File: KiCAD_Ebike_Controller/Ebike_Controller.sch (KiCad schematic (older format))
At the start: 1 part

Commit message: close to being done, need to add current pull ups on i2c
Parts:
- removed J?: Conn_01x05_Male, symbol Connector:Conn_01x05_Male
- added J?: Conn_01x05_Male, symbol Connector:Conn_01x05_Male
- added J?: SWD Programming Pins, symbol Connector:Conn_01x05_Male
- added R?: 100k, symbol Device:R_Small
- added SW?: SW_Push, symbol Switch:SW_Push
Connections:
- net labels added: +48V, LSS
- wire segments 37 -> 65

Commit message: schem done
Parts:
- removed SW?: SW_Push, symbol Switch:SW_Push
- added C? (x2): 100n, symbol Device:C_Small
- added J?: Mode 2, symbol Connector:Conn_01x02_Female
- added J?: Mode 1, symbol Connector:Conn_01x02_Female
- added R?: 100k, symbol Device:R_Small
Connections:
- net labels added: BRAKE_SW_BP6, SWCLK, SWDIO, THROTTLE_PA2, nRST
- wire segments 65 -> 87
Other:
- moved on the sheet: R?

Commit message: adding footprints
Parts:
- removed J?: Conn_01x05_Male, symbol Connector:Conn_01x05_Male
- removed J?: SWD Programming Pins, symbol Connector:Conn_01x05_Male
- removed J?: Mode 2, symbol Connector:Conn_01x02_Female
- removed J?: Mode 1, symbol Connector:Conn_01x02_Female
- added C1: 100n, Capacitor_SMD:C_0805_2012Metric, symbol Device:C_Small
- added J1: IO, symbol Connector:Conn_01x06_Female
- added J2: Prog, symbol Connector:Conn_01x05_Female
- added J3: Hall Effect Sensors, symbol Connector:Screw_Terminal_01x05
- added J4: PHASE_A, symbol Connector:Screw_Terminal_01x01
- added J5: PHASE_B, symbol Connector:Screw_Terminal_01x01
- added J6: PHASE_C, symbol Connector:Screw_Terminal_01x01
- added R1: 100k, symbol Device:R_Small
- C2, C3: renamed from C?; footprint (none) -> Capacitor_SMD:C_0805_2012Metric_Pad1.15x1.40mm_HandSolder
- gave numbers to parts that had none: 2
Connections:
- net labels added: MODE1_SW_PB7, MODE2_SW_PA3
- wire segments 87 -> 88
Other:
- note added: "A"
- note added: "B"
- note added: "C"
- note added: "IO Pins"
- note added: "debounce filters"
- moved on the sheet: C2, C3, R2, R3

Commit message: 50% of the way through the layout
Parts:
- added C32: 50n, Capacitor_SMD:C_0805_2012Metric_Pad1.15x1.40mm_HandSolder, symbol Device:C_Small
- added J8: +48V, Power_Connector:180A_screw_terminal_7461383, symbol Connector:Screw_Terminal_01x01
- added J9: GND, Power_Connector:180A_screw_terminal_7461383, symbol Connector:Screw_Terminal_01x01
- added NT1: Net-Tie_3, NetTie:NetTie-3_THT_Pad1.0mm, symbol Device:Net-Tie_3
- added R45: 8.2k, Resistor_SMD:R_0805_2012Metric_Pad1.15x1.40mm_HandSolder, symbol Device:R_Small
- C1: footprint Capacitor_SMD:C_0805_2012Metric -> Capacitor_SMD:C_0805_2012Metric_Pad1.15x1.40mm_HandSolder
- J1: footprint (none) -> Connector_PinHeader_2.54mm:PinHeader_1x06_P2.54mm_Vertical
- J2: footprint (none) -> Connector_PinHeader_2.54mm:PinHeader_1x05_P2.54mm_Vertical
- J3: footprint (none) -> Connector_Phoenix_MC:PhoenixContact_MC_1,5_5-G-3.81_1x05_P3.81mm_Horizontal
- J4, J5, J6: footprint (none) -> Power_Connector:180A_screw_terminal_7461383
- R1, R2, R3: footprint (none) -> Resistor_SMD:R_0805_2012Metric_Pad1.15x1.40mm_HandSolder
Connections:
- net +48V: now also J8.1 (Pin_1)
- net GND: now also J9.1 (Pin_1), NT1.2; no longer C1.2, C2.2, C3.2, J1.6 (Pin_6), J2.5 (Pin_5), J3.5 (Pin_5)
- net MODE1_SW_PB7: now also J1.4 (Pin_4); no longer J1.5 (Pin_5)
- net MODE2_SW_PA3: now also J1.5 (Pin_5); no longer J1.4 (Pin_4)
- net THROTTLE_PA2: now also R45.1
- new net GNDA: C1.2, C2.2, C3.2, C32.2, NT1.1
- new net GNDD: J1.6 (Pin_6), J2.5 (Pin_5), J3.5 (Pin_5), NT1.3
- new net MCU/THROTTLE_PA2: C32.1, R45.2
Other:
- note added: "Battery\nInputs"
- note added: "Star ground connections"
- note added: "THROTTLE_PA2"
- note added: "low pass filter"
- moved on the sheet: C1, C2, C3, J1, R1, R2, R3

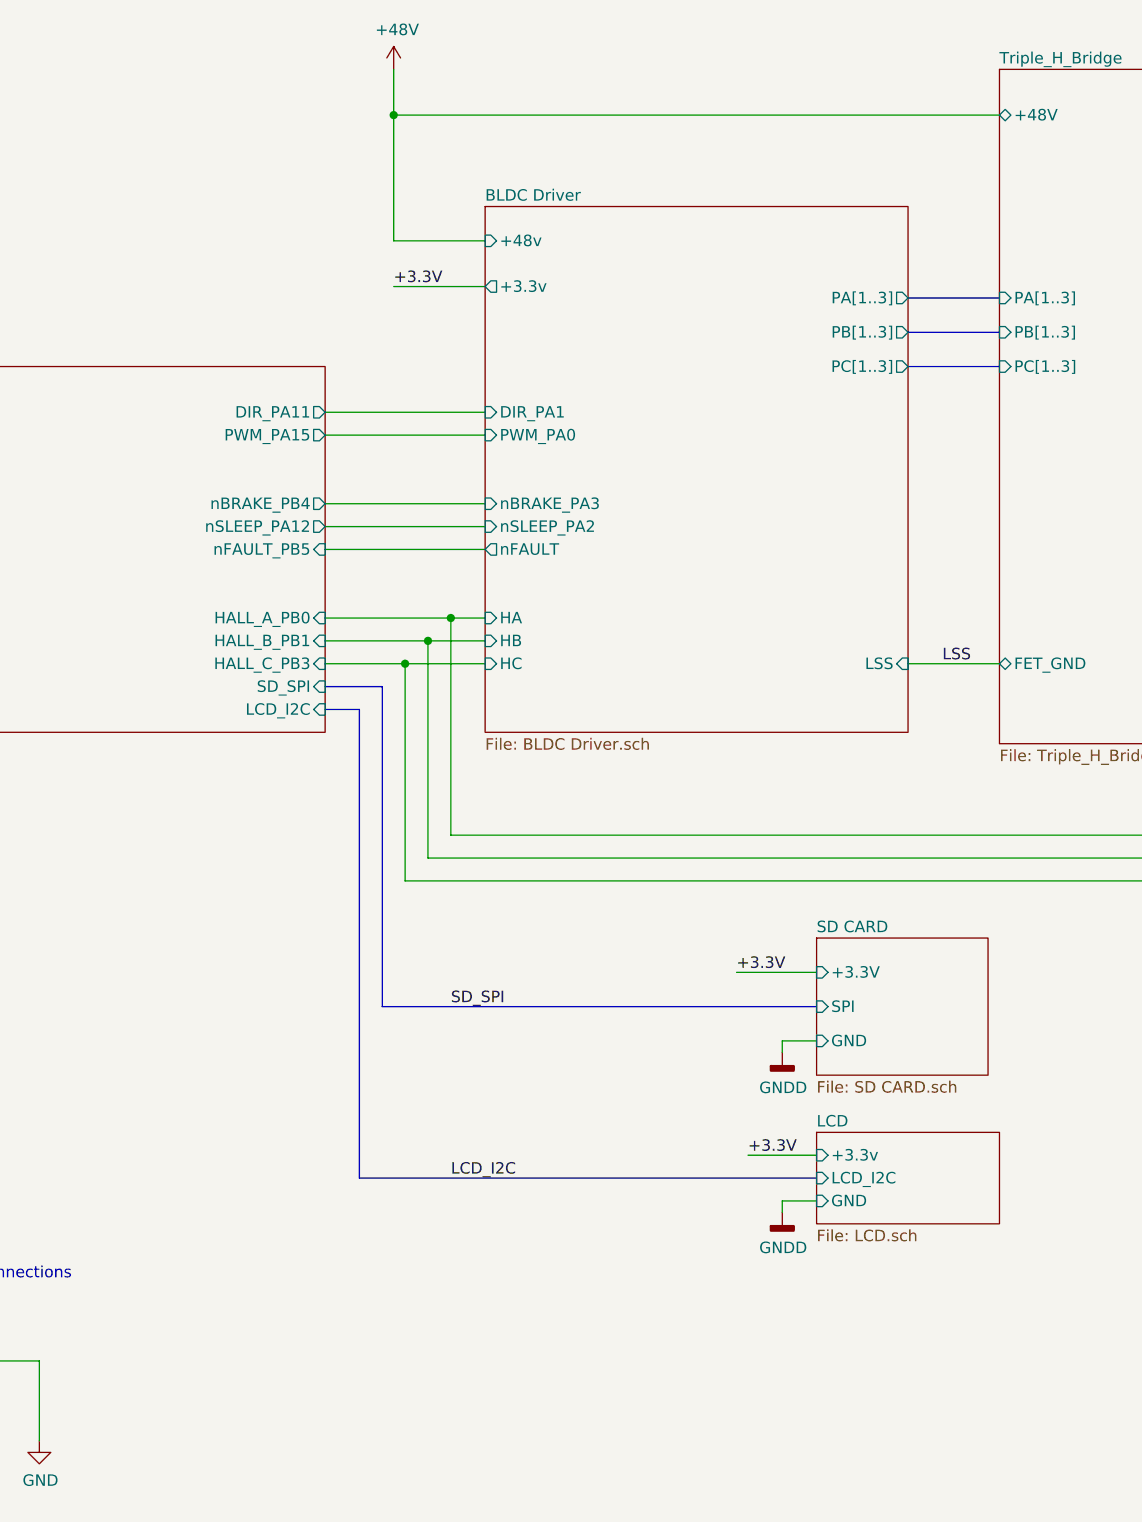
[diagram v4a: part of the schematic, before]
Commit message: Layout done. will tidy up ref des next
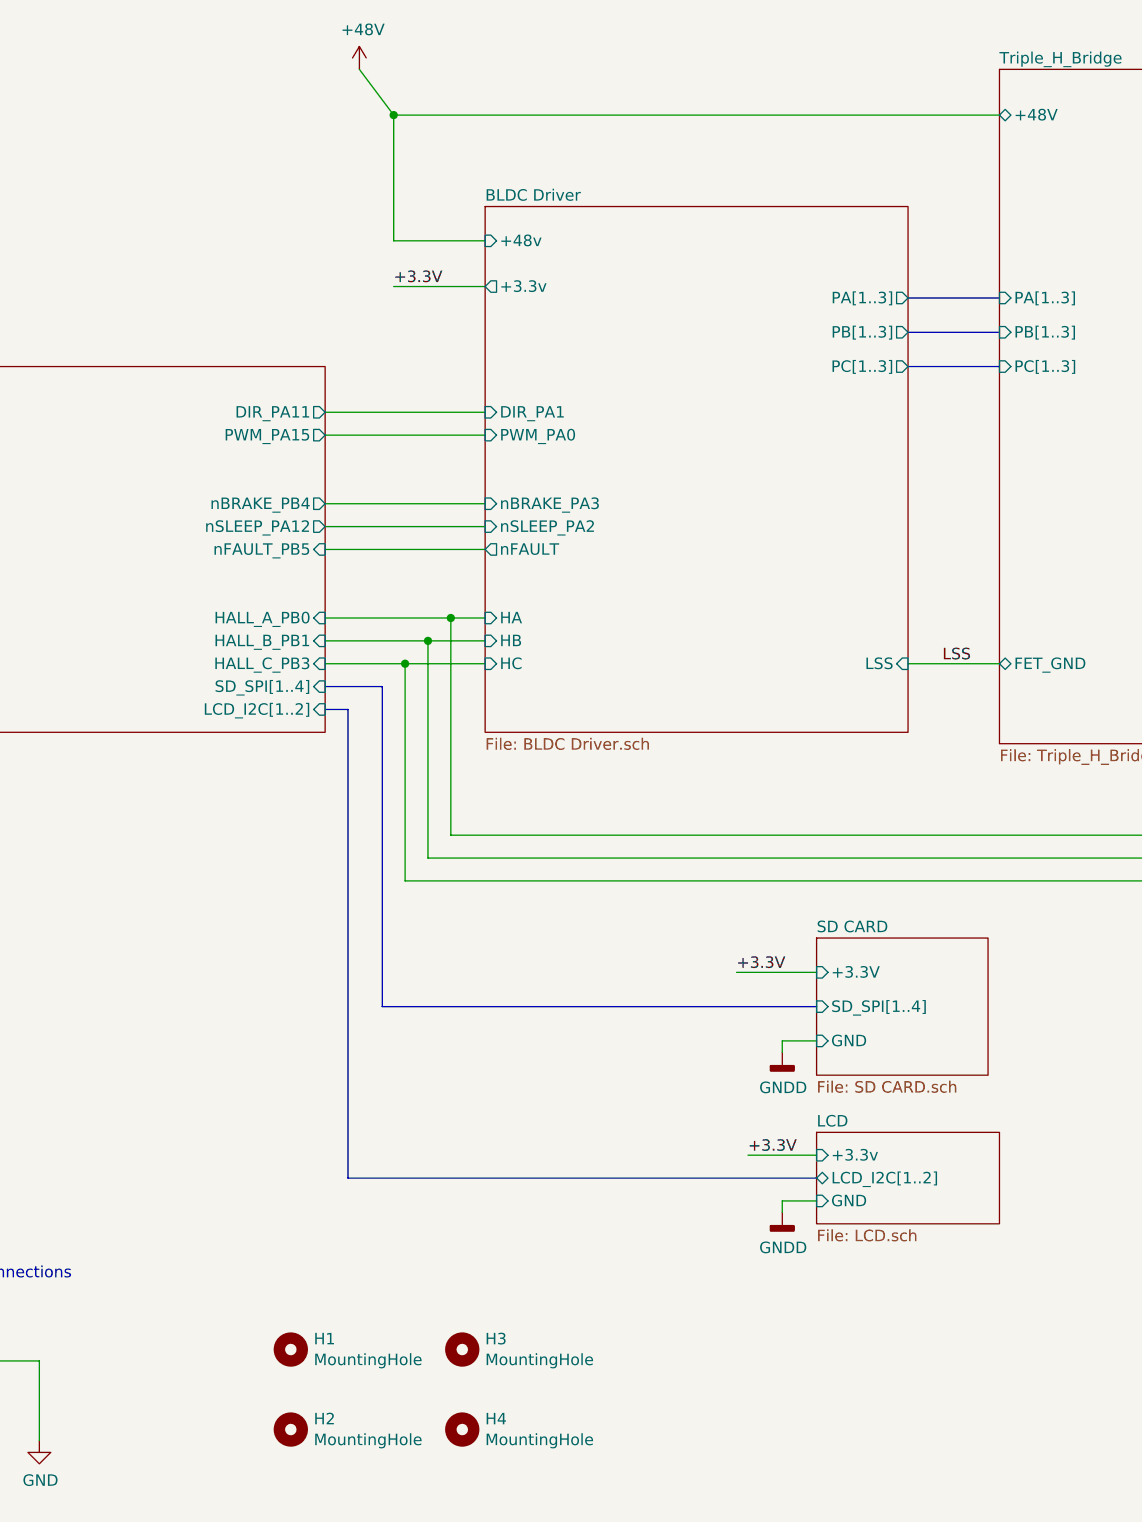
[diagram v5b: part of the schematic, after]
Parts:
- added H1, H2: MountingHole, MountingHole:MountingHole_3.2mm_M3, symbol Mechanical:MountingHole
- added H3, H4: MountingHole, MountingHole:MountingHole_3.2mm_M3_DIN965, symbol Mechanical:MountingHole
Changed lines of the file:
@@
 Wire Wire Line
 	5550 3300 6250 3300
-$Sheet
-S 3400 2500 2150 1600
-U 5F8BD648
-F0 "MCU" 50
-F1 "MCU.sch" 50
-F2 "+3.3v" I L 3400 2650 50
-F3 "GND" I L 3400 3850 50
-F4 "PWM_PA15" O R 5550 2800 50
-F5 "DIR_PA11" O R 5550 2700 50
-F6 "nSLEEP_PA12" O R 5550 3200 50
-F7 "V_BATT_MON_PA0" I L 3400 2750 50
-F8 "I_BATT_MON_PA1" I L 3400 2850 50
-F9 "THROTTLE_PA2" I L 3400 3050 50
-F10 "SD_SPI" I R 5550 3900 50
-F11 "LCD_I2C" I R 5550 4000 50
-F12 "HALL_A_PB0" I R 5550 3600 50
-F13 "HALL_B_PB1" I R 5550 3700 50
-F14 "nRST" I L 3400 3450 50
-F15 "MODE2_SW_PA3" I L 3400 3200 50
-F16 "HALL_C_PB3" I R 5550 3800 50
-F17 "nBRAKE_PB4" O R 5550 3100 50
-F18 "nFAULT_PB5" I R 5550 3300 50
-F19 "SWDIO_PA13" O L 3400 3550 50
-F20 "SWCLK_PA14" O L 3400 3650 50
-F21 "BRAKE_SW_PB6" I L 3400 2950 50
-F22 "MODE1_SW_PB7" I L 3400 3300 50
-$EndSheet
 Wire Wire Line
 	6100 4550 10050 4550
@@
 Wire Bus Line
 	5800 5300 7700 5300
-Wire Bus Line
-	5550 4000 5700 4000
-Text Label 6100 5300 0    50   ~ 0
-SD_SPI
-Text Label 6100 6050 0    50   ~ 0
-LCD_I2C
 $Sheet
 S 7700 5850 800  400
@@
 F0 "LCD" 50
 F1 "LCD.sch" 50
-F2 "LCD_I2C" I L 7700 6050 50
+F2 "LCD_I2C[1..2]" B L 7700 6050 50
 F3 "+3.3v" I L 7700 5950 50
 F4 "GND" I L 7700 6150 50
@@
 	1100 1650 850  1650
 Wire Wire Line
-	5850 1200 5850 1400
+	5700 1200 5850 1400
 Wire Wire Line
 	850  1200 850  1550
@@
 L power:+48V #PWR0105
 U 1 1 5FB22E4A
-P 5850 1200
-F 0 "#PWR0105" H 5850 1050 50  0001 C CNN
-F 1 "+48V" H 5865 1373 50  0000 C CNN
-F 2 "" H 5850 1200 50  0001 C CNN
-F 3 "" H 5850 1200 50  0001 C CNN
-	1    5850 1200
+P 5700 1200
+F 0 "#PWR0105" H 5700 1050 50  0001 C CNN
+F 1 "+48V" H 5715 1373 50  0000 C CNN
+F 2 "" H 5700 1200 50  0001 C CNN
+F 3 "" H 5700 1200 50  0001 C CNN
+	1    5700 1200
 	1    0    0    -1
 $EndComp
@@
 F1 "SD CARD.sch" 50
 F2 "GND" I L 7700 5450 50
-F3 "SPI" I L 7700 5300 50
+F3 "SD_SPI[1..4]" I L 7700 5300 50
 F4 "+3.3V" I L 7700 5150 50
 $EndSheet
-Wire Bus Line
-	5700 4000 5700 6050
-Wire Bus Line
-	5700 6050 7700 6050
 Wire Wire Line
 	8500 1400 5850 1400
@@
 	-1   0    0    -1
 $EndComp
+Wire Bus Line
+	5650 6050 5650 4000
+Wire Bus Line
+	5650 4000 5550 4000
+Wire Bus Line
+	5650 6050 7700 6050
+$Sheet
+S 3400 2500 2150 1600
+U 5F8BD648
+F0 "MCU" 50
+F1 "MCU.sch" 50
+F2 "+3.3v" I L 3400 2650 50
+F3 "GND" I L 3400 3850 50
+F4 "PWM_PA15" O R 5550 2800 50
+F5 "DIR_PA11" O R 5550 2700 50
+F6 "nSLEEP_PA12" O R 5550 3200 50
+F7 "V_BATT_MON_PA0" I L 3400 2750 50
+F8 "I_BATT_MON_PA1" I L 3400 2850 50
+F9 "THROTTLE_PA2" I L 3400 3050 50
+F10 "SD_SPI[1..4]" I R 5550 3900 50
+F11 "HALL_A_PB0" I R 5550 3600 50
+F12 "HALL_B_PB1" I R 5550 3700 50
+F13 "nRST" I L 3400 3450 50
+F14 "MODE2_SW_PA3" I L 3400 3200 50
+F15 "HALL_C_PB3" I R 5550 3800 50
+F16 "nBRAKE_PB4" O R 5550 3100 50
+F17 "nFAULT_PB5" I R 5550 3300 50
+F18 "SWDIO_PA13" O L 3400 3550 50
+F19 "SWCLK_PA14" O L 3400 3650 50
+F20 "BRAKE_SW_PB6" I L 3400 2950 50
+F21 "MODE1_SW_PB7" I L 3400 3300 50
+F22 "LCD_I2C[1..2]" I R 5550 4000 50
+$EndSheet
+$Comp
+L Mechanical:MountingHole H1
+U 1 1 600BEACE
+P 5400 6800
+F 0 "H1" H 5500 6846 50  0000 L CNN
+F 1 "MountingHole" H 5500 6755 50  0000 L CNN
+F 2 "MountingHole:MountingHole_3.2mm_M3" H 5400 6800 50  0001 C CNN
+F 3 "~" H 5400 6800 50  0001 C CNN
+	1    5400 6800
+	1    0    0    -1
+$EndComp
+$Comp
+L Mechanical:MountingHole H3
+U 1 1 600BFB0E
+P 6150 6800
+F 0 "H3" H 6250 6846 50  0000 L CNN
+F 1 "MountingHole" H 6250 6755 50  0000 L CNN
+F 2 "MountingHole:MountingHole_3.2mm_M3_DIN965" H 6150 6800 50  0001 C CNN
+F 3 "~" H 6150 6800 50  0001 C CNN
+	1    6150 6800
+	1    0    0    -1
+$EndComp
+$Comp
+L Mechanical:MountingHole H4
+U 1 1 600BFEEB
+P 6150 7150
+F 0 "H4" H 6250 7196 50  0000 L CNN
+F 1 "MountingHole" H 6250 7105 50  0000 L CNN
+F 2 "MountingHole:MountingHole_3.2mm_M3_DIN965" H 6150 7150 50  0001 C CNN
+F 3 "~" H 6150 7150 50  0001 C CNN
+	1    6150 7150
+	1    0    0    -1
+$EndComp
+$Comp
+L Mechanical:MountingHole H2
+U 1 1 600C0109
+P 5400 7150
+F 0 "H2" H 5500 7196 50  0000 L CNN
+F 1 "MountingHole" H 5500 7105 50  0000 L CNN
+F 2 "MountingHole:MountingHole_3.2mm_M3" H 5400 7150 50  0001 C CNN
+F 3 "~" H 5400 7150 50  0001 C CNN
+	1    5400 7150
+	1    0    0    -1
+$EndComp
 $EndSCHEMATC

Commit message: Finished ready for fab
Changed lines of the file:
@@
 	1100 1650 850  1650
 Wire Wire Line
-	5700 1200 5850 1400
+	5850 1200 5850 1400
 Wire Wire Line
 	850  1200 850  1550
@@
 L power:+48V #PWR0105
 U 1 1 5FB22E4A
-P 5700 1200
-F 0 "#PWR0105" H 5700 1050 50  0001 C CNN
-F 1 "+48V" H 5715 1373 50  0000 C CNN
-F 2 "" H 5700 1200 50  0001 C CNN
-F 3 "" H 5700 1200 50  0001 C CNN
-	1    5700 1200
+P 5850 1200
+F 0 "#PWR0105" H 5850 1050 50  0001 C CNN
+F 1 "+48V" H 5865 1373 50  0000 C CNN
+F 2 "" H 5850 1200 50  0001 C CNN
+F 3 "" H 5850 1200 50  0001 C CNN
+	1    5850 1200
 	1    0    0    -1
 $EndComp

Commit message: done and gerbes sent to JLC
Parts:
- added D11, D12, D13: STPS2L60ZFY, Diode_SMD:D_SOD-123, symbol Device:D_Small
- added SW2: SW_SPST, Connector_PinHeader_2.54mm:PinHeader_1x02_P2.54mm_Vertical, symbol Switch:SW_SPST
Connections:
- net +3.3V: now also D11.1 (K); no longer J2.1 (Pin_1)
- net BMS/V_BATT_MON_PA0: now also SW2.1 (A)
- new net: D11.2 (A), J2.1 (Pin_1)
- new net: D12.2 (A), SW2.2 (B)
- new net BLDC Driver/nSLEEP_PA12: D12.1 (K), D13.1 (K)
- new net MCU/nSLEEP_PA12: D13.2 (A)
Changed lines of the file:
@@
 	8100 2350 8500 2350
 Wire Wire Line
-	5850 1400 5850 1950
-Wire Wire Line
-	5850 1950 6250 1950
+	6000 1400 6000 1950
+Wire Wire Line
+	6000 1950 6250 1950
 Wire Wire Line
 	5550 2700 6250 2700
 Wire Wire Line
 	5550 2800 6250 2800
-Wire Wire Line
-	5550 3200 6250 3200
 Wire Wire Line
 	6250 3100 5550 3100
@@
 	1100 1650 850  1650
 Wire Wire Line
-	5850 1200 5850 1400
+	6000 1200 6000 1400
 Wire Wire Line
 	850  1200 850  1550
@@
 Wire Wire Line
 	1550 6950 1900 6950
-Wire Wire Line
-	1550 6550 1900 6550
 Text Notes 800  6850 0    50   ~ 0
 SWD\nProgramming\nInput
@@
 	7550 5450 7550 5500
 Wire Wire Line
-	6250 2150 5850 2150
-Text Label 5850 2150 0    50   ~ 0
+	6250 2150 6000 2150
+Text Label 6000 2150 0    50   ~ 0
 +3.3V
 $Comp
 L power:+48V #PWR0105
 U 1 1 5FB22E4A
-P 5850 1200
-F 0 "#PWR0105" H 5850 1050 50  0001 C CNN
-F 1 "+48V" H 5865 1373 50  0000 C CNN
-F 2 "" H 5850 1200 50  0001 C CNN
-F 3 "" H 5850 1200 50  0001 C CNN
-	1    5850 1200
+P 6000 1200
+F 0 "#PWR0105" H 6000 1050 50  0001 C CNN
+F 1 "+48V" H 6015 1373 50  0000 C CNN
+F 2 "" H 6000 1200 50  0001 C CNN
+F 3 "" H 6000 1200 50  0001 C CNN
+	1    6000 1200
 	1    0    0    -1
 $EndComp
@@
 Wire Wire Line
 	3400 2750 2800 2750
-Wire Wire Line
-	2800 2750 2800 1700
 Wire Wire Line
 	2800 1700 2300 1700
@@
 	-1   0    0    1
 $EndComp
-Wire Wire Line
-	1550 5450 1900 5450
 Wire Wire Line
 	1900 5450 1900 5250
@@
 $EndSheet
 Wire Wire Line
-	8500 1400 5850 1400
-Connection ~ 5850 1400
+	8500 1400 6000 1400
+Connection ~ 6000 1400
 $Comp
 L Connector:Conn_01x06_Female J1
@@
 F3 "HB" I L 6250 3700 50
 F4 "HA" I L 6250 3600 50
-F5 "nSLEEP_PA2" I L 6250 3200 50
+F5 "nSLEEP_PA12" I L 6250 3200 50
 F6 "nBRAKE_PA3" I L 6250 3100 50
 F7 "PWM_PA0" I L 6250 2800 50
@@
 	1    0    0    -1
 $EndComp
+$Comp
+L Device:D_Small D?
+U 1 1 60355900
+P 1750 6550
+AR Path="/5F8D3A83/60355900" Ref="D?"  Part="1"
+AR Path="/60355900" Ref="D11"  Part="1"
+F 0 "D11" H 1700 6650 50  0000 L CNN
+F 1 "STPS2L60ZFY" H 1150 6650 50  0000 L CNN
+F 2 "Diode_SMD:D_SOD-123" V 1750 6550 50  0001 C CNN
+F 3 "~" V 1750 6550 50  0001 C CNN
+	1    1750 6550
+	-1   0    0    -1
+$EndComp
+Wire Wire Line
+	1650 6550 1550 6550
+Wire Wire Line
+	1850 6550 1900 6550
+Wire Wire Line
+	1550 5450 1900 5450
+Wire Wire Line
+	2800 2750 2800 1700
+Wire Wire Line
+	3950 1700 2800 1700
+Connection ~ 2800 1700
+$Comp
+L Device:D_Small D?
+U 1 1 6038D2A5
+P 4900 1700
+AR Path="/5F8D3A83/6038D2A5" Ref="D?"  Part="1"
+AR Path="/6038D2A5" Ref="D12"  Part="1"
+F 0 "D12" H 4850 1900 50  0000 L CNN
+F 1 "STPS2L60ZFY" H 4650 1800 50  0000 L CNN
+F 2 "Diode_SMD:D_SOD-123" V 4900 1700 50  0001 C CNN
+F 3 "~" V 4900 1700 50  0001 C CNN
+	1    4900 1700
+	-1   0    0    1
+$EndComp
+Wire Wire Line
+	4350 1700 4800 1700
+$Comp
+L Device:D_Small D?
+U 1 1 60394A18
+P 5650 3200
+AR Path="/5F8D3A83/60394A18" Ref="D?"  Part="1"
+AR Path="/60394A18" Ref="D13"  Part="1"
+F 0 "D13" H 5600 3500 50  0000 L CNN
+F 1 "STPS2L60ZFY" H 5350 3400 50  0000 L CNN
+F 2 "Diode_SMD:D_SOD-123" V 5650 3200 50  0001 C CNN
+F 3 "~" V 5650 3200 50  0001 C CNN
+	1    5650 3200
+	-1   0    0    1
+$EndComp
+Wire Wire Line
+	5750 3200 5800 3200
+Wire Wire Line
+	5800 3200 5800 1700
+Connection ~ 5800 3200
+Wire Wire Line
+	5800 3200 6250 3200
+Wire Wire Line
+	5000 1700 5800 1700
+$Comp
+L Switch:SW_SPST SW2
+U 1 1 5FFB1A1D
+P 4150 1700
+F 0 "SW2" H 4150 1935 50  0000 C CNN
+F 1 "SW_SPST" H 4150 1844 50  0000 C CNN
+F 2 "Connector_PinHeader_2.54mm:PinHeader_1x02_P2.54mm_Vertical" H 4150 1700 50  0001 C CNN
+F 3 "~" H 4150 1700 50  0001 C CNN
+	1    4150 1700
+	1    0    0    -1
+$EndComp
